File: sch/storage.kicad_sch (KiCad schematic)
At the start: 6 parts, among them J2 Micro_SD_Card, U3 ATF1504AS-xAx44, U4 74LVC125

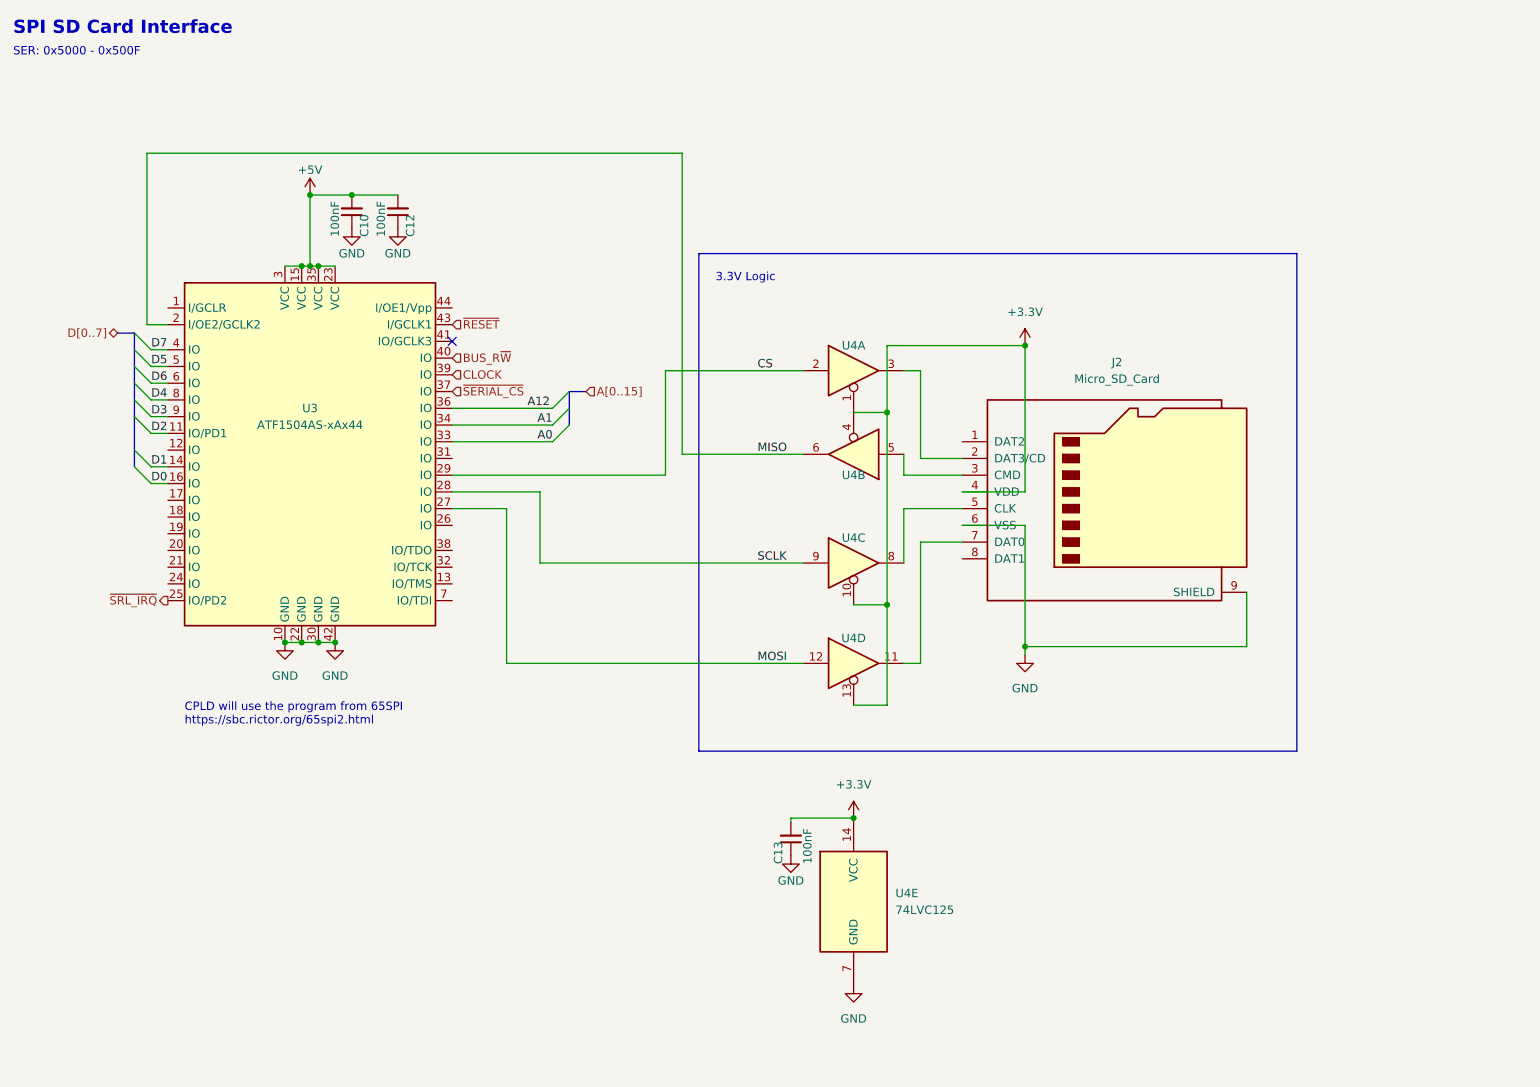
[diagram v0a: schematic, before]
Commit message: fix peripherals, add SPI
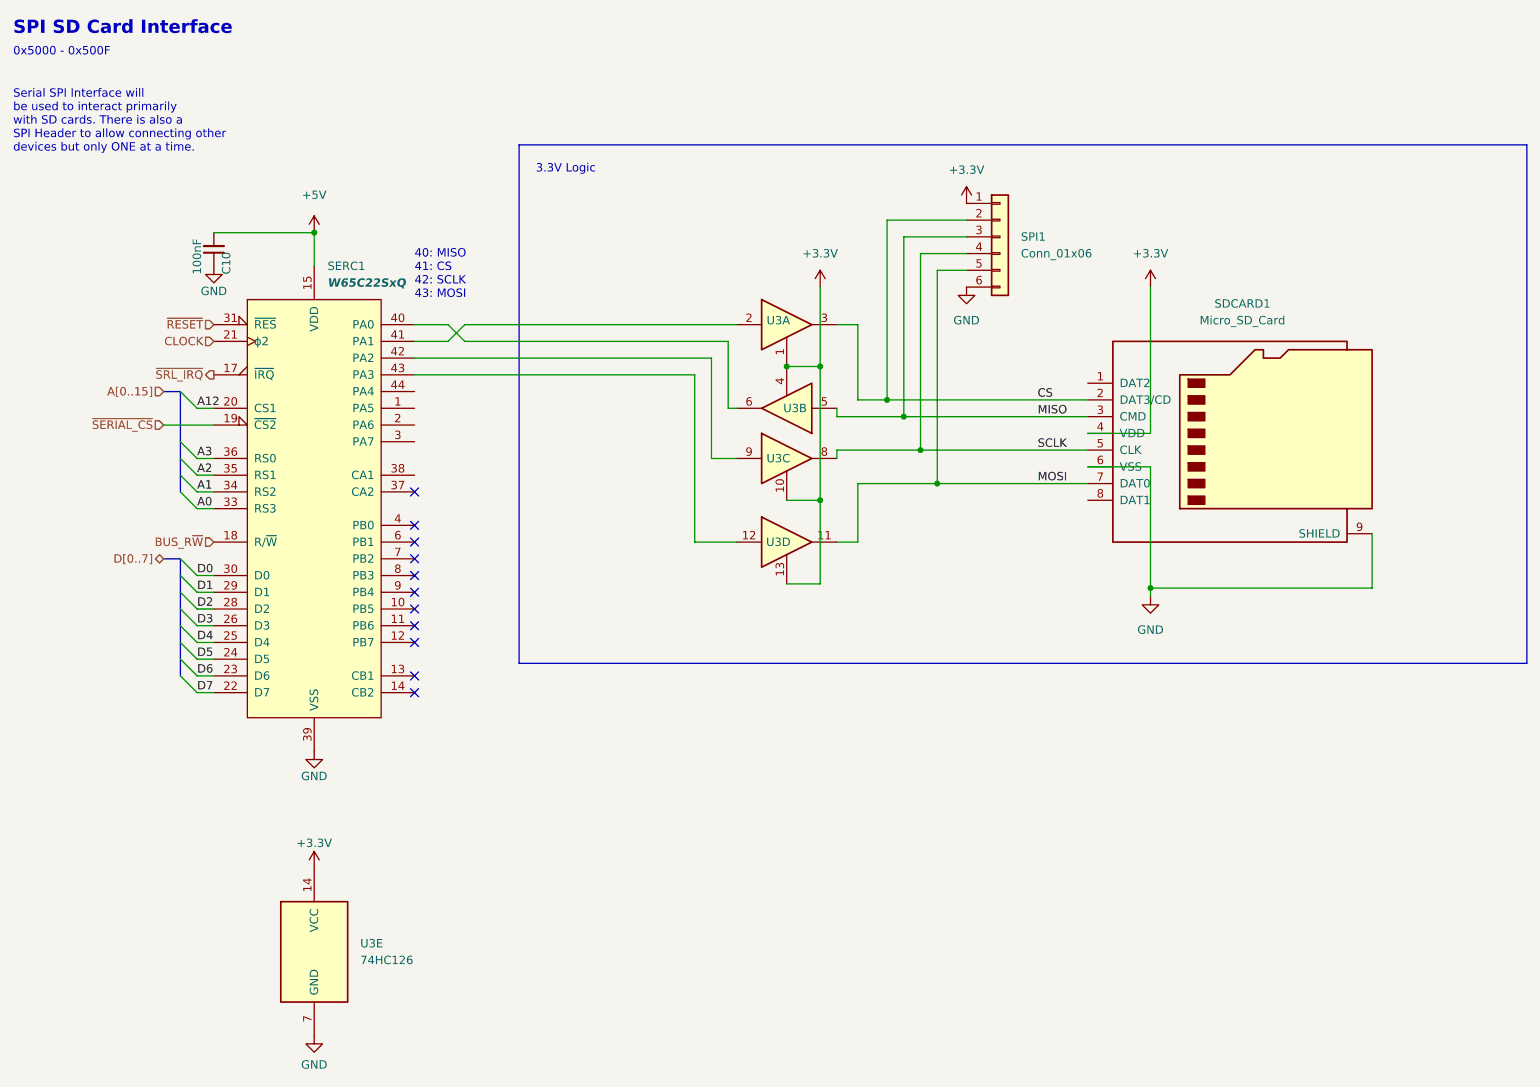
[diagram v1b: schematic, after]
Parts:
- removed C12, C13: 100nF, Capacitor_SMD:C_0805_2012Metric, symbol Device:C_Small
- removed U3: ATF1504AS-xAx44, Package_LCC:PLCC-44, symbol CPLD_Microchip:ATF1504AS-xAx44
- removed U4: 74LVC125, symbol 74xx:74LVC125
- added SERC1: W65C22SxQ, Package_QFP:PQFP-44_10x10mm_P0.8mm, symbol 65xx:W65C22SxQ
- added SPI1: Conn_01x06, Connector_PinHeader_2.00mm:PinHeader_1x06_P2.00mm_Vertical, symbol Connector_Generic:Conn_01x06
- added U3: 74HC126, symbol 74xx:74LS126
- renumbered J2 to SDCARD1
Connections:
- net +3V3: now also SPI1.1 (Pin_1), U3.1, U3.10, U3.13, U3.14 (VCC), U3.4
- net +5V: now also SERC1.15 (VDD)
- net A0: now also SERC1.33 (RS3)
- net A1: now also SERC1.34 (RS2)
- net A12: now also SERC1.20 (CS1)
- net BUS_R~{W}: now also SERC1.18 (R/~{W})
- net CLOCK: now also SERC1.21 (ϕ2)
- net CS: now also SDCARD1.2 (DAT3/CD), SPI1.2 (Pin_2), U3.3
- net D0: now also SERC1.30 (D0)
- net D1: now also SERC1.29 (D1)
- net D2: now also SERC1.28 (D2)
- net D3: now also SERC1.26 (D3)
- net D4: now also SERC1.25 (D4)
- net D5: now also SERC1.24 (D5)
- net D6: now also SERC1.23 (D6)
- net D7: now also SERC1.22 (D7)
- net GND: now also SERC1.39 (VSS), SPI1.6 (Pin_6), U3.7 (GND)
- net MISO: now also SDCARD1.3 (CMD), SPI1.3 (Pin_3), U3.5
- net MOSI: now also SDCARD1.7 (DAT0), SPI1.5 (Pin_5), U3.11
- net SCLK: now also SDCARD1.5 (CLK), SPI1.4 (Pin_4), U3.8
- net ~{RESET}: now also SERC1.31 (~{RES})
- net ~{SERIAL_CS}: now also SERC1.19 (~{CS2})
- net ~{SRL_IRQ}: now also SERC1.17 (~{IRQ})
- new net: SERC1.43 (PA3), U3.12
- new net: SERC1.40 (PA0), U3.6
- new net: SERC1.41 (PA1), U3.2
- new net: SERC1.42 (PA2), U3.9
- new net A2: SERC1.35 (RS1)
- new net A3: SERC1.36 (RS0)
- no-connect marks 1 -> 11
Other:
- note added: "0x5000 - 0x500F"
- note added: "40: MISO 41: CS 42: SCLK 43: MOSI"
- note added: "Serial SPI Interface will be used to interact primarily with SD cards. There is also a SPI Header to allow connecting other devices but only ONE at a time."
- note removed: "CPLD will use the program from 65SPI https://sbc.rictor.org/65spi2.html"
- note removed: "SER: 0x5000 - 0x500F"
- moved on the sheet: C10, SDCARD1

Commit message: Cleanup board
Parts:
- U3: value 74HC126 -> (none)
- U3: value 74HC126 -> (none); footprint Package_SO:SOIC-14_3.9x8.7mm_P1.27mm -> (none)
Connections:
- no-connect marks 11 -> 18
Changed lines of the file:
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@@
   (no_connect (at 86.36 109.855))
   (no_connect (at 86.36 112.395))
+  (no_connect (at 86.36 94.615))
+  (no_connect (at 86.36 81.915))
+  (no_connect (at 86.36 84.455))
+  (no_connect (at 86.36 86.995))
+  (no_connect (at 86.36 89.535))
+  (no_connect (at 188.595 98.425))
+  (no_connect (at 188.595 80.645))
   (bus_entry (at 50.8 122.555) (size 2.54 2.54)
     (stroke (width 0) (type default) (color 0 0 0 0))
@@
     (stroke (width 0) (type default) (color 0 0 0 0))
   )
-  (wire (pts (xy 131.445 76.835) (xy 131.445 92.075))
+  (wire (pts (xy 132.715 76.835) (xy 132.715 92.075))
     (stroke (width 0) (type default) (color 0 0 0 0))
   )
@@
     (stroke (width 0) (type default) (color 0 0 0 0))
   )
-  (wire (pts (xy 131.445 92.075) (xy 135.255 92.075))
+  (wire (pts (xy 132.715 92.075) (xy 135.255 92.075))
     (stroke (width 0) (type default) (color 0 0 0 0))
   )
@@
     (stroke (width 0) (type default) (color 0 0 0 0))
   )
-  (wire (pts (xy 86.36 79.375) (xy 128.905 79.375))
+  (wire (pts (xy 86.36 79.375) (xy 130.175 79.375))
     (stroke (width 0) (type default) (color 0 0 0 0))
   )
@@
     (stroke (width 0) (type default) (color 0 0 0 0))
   )
-  (wire (pts (xy 133.985 84.455) (xy 135.255 84.455))
-    (stroke (width 0) (type default) (color 0 0 0 0))
-  )
   (wire (pts (xy 165.735 95.885) (xy 188.595 95.885))
     (stroke (width 0) (type default) (color 0 0 0 0))
   )
-  (wire (pts (xy 128.905 79.375) (xy 128.905 104.775))
+  (wire (pts (xy 130.175 79.375) (xy 130.175 104.775))
     (stroke (width 0) (type default) (color 0 0 0 0))
   )
@@
     (stroke (width 0) (type default) (color 0 0 0 0))
   )
-  (wire (pts (xy 86.36 76.835) (xy 131.445 76.835))
+  (wire (pts (xy 86.36 76.835) (xy 132.715 76.835))
     (stroke (width 0) (type default) (color 0 0 0 0))
   )
@@
     (stroke (width 0) (type default) (color 0 0 0 0))
   )
-  (wire (pts (xy 133.985 74.295) (xy 133.985 84.455))
+  (wire (pts (xy 135.255 74.295) (xy 135.255 84.455))
     (stroke (width 0) (type default) (color 0 0 0 0))
   )
@@
     (stroke (width 0) (type default) (color 0 0 0 0))
   )
-  (wire (pts (xy 128.905 104.775) (xy 135.255 104.775))
+  (wire (pts (xy 130.175 104.775) (xy 135.255 104.775))
     (stroke (width 0) (type default) (color 0 0 0 0))
   )
@@
     (stroke (width 0) (type default) (color 0 0 0 0))
   )
-  (wire (pts (xy 93.98 74.295) (xy 133.985 74.295))
+  (wire (pts (xy 93.98 74.295) (xy 135.255 74.295))
     (stroke (width 0) (type default) (color 0 0 0 0))
   )
@@
     (in_bom yes) (on_board yes)
     (property "Reference" "U3" (id 0) (at 141.605 104.775 0))
-    (property "Value" "74HC126" (id 1) (at 142.875 98.425 0)
+    (property "Value" "" (id 1) (at 142.875 98.425 0)
       (effects (font (size 1.27 1.27)) hide)
     )
@@
       (effects (font (size 1.27 1.27)) hide)
     )
-    (property "Datasheet" "http://www.ti.com/lit/gpn/sn74LS126" (id 3) (at 142.875 104.775 0)
+    (property "Datasheet" "https://www.ti.com/lit/ds/symlink/sn74lvc126a.pdf" (id 3) (at 142.875 104.775 0)
       (effects (font (size 1.27 1.27)) hide)
     )
@@
     (in_bom yes) (on_board yes)
     (property "Reference" "U3" (id 0) (at 144.145 84.455 0))
-    (property "Value" "74HC126" (id 1) (at 142.875 90.805 0)
+    (property "Value" "" (id 1) (at 142.875 90.805 0)
       (effects (font (size 1.27 1.27)) hide)
     )
@@
       (effects (font (size 1.27 1.27)) hide)
     )
-    (property "Datasheet" "http://www.ti.com/lit/gpn/sn74LS126" (id 3) (at 142.875 84.455 0)
+    (property "Datasheet" "https://www.ti.com/lit/ds/symlink/sn74lvc126a.pdf" (id 3) (at 142.875 84.455 0)
       (effects (font (size 1.27 1.27)) hide)
     )
@@
     (in_bom yes) (on_board yes)
     (property "Reference" "U3" (id 0) (at 141.605 71.12 0))
-    (property "Value" "74HC126" (id 1) (at 142.875 64.77 0)
+    (property "Value" "" (id 1) (at 142.875 64.77 0)
       (effects (font (size 1.27 1.27)) hide)
     )
@@
       (effects (font (size 1.27 1.27)) hide)
     )
-    (property "Datasheet" "http://www.ti.com/lit/gpn/sn74LS126" (id 3) (at 142.875 71.755 0)
+    (property "Datasheet" "https://www.ti.com/lit/ds/symlink/sn74lvc126a.pdf" (id 3) (at 142.875 71.755 0)
       (effects (font (size 1.27 1.27)) hide)
     )
@@
       (effects (font (size 1.27 1.27)) (justify left))
     )
-    (property "Value" "74HC126" (id 1) (at 78.105 168.2749 0)
+    (property "Value" "" (id 1) (at 78.105 168.2749 0)
       (effects (font (size 1.27 1.27)) (justify left))
     )
-    (property "Footprint" "Package_SO:SOIC-14_3.9x8.7mm_P1.27mm" (id 2) (at 71.12 167.005 0)
-      (effects (font (size 1.27 1.27)) hide)
-    )
-    (property "Datasheet" "http://www.ti.com/lit/gpn/sn74LS126" (id 3) (at 71.12 167.005 0)
+    (property "Footprint" "" (id 2) (at 71.12 167.005 0)
+      (effects (font (size 1.27 1.27)) hide)
+    )
+    (property "Datasheet" "https://www.ti.com/lit/ds/symlink/sn74lvc126a.pdf" (id 3) (at 71.12 167.005 0)
       (effects (font (size 1.27 1.27)) hide)
     )
@@
     (in_bom yes) (on_board yes)
     (property "Reference" "U3" (id 0) (at 141.605 92.075 0))
-    (property "Value" "74HC126" (id 1) (at 142.875 85.725 0)
+    (property "Value" "" (id 1) (at 142.875 85.725 0)
       (effects (font (size 1.27 1.27)) hide)
     )
@@
       (effects (font (size 1.27 1.27)) hide)
     )
-    (property "Datasheet" "http://www.ti.com/lit/gpn/sn74LS126" (id 3) (at 142.875 92.075 0)
-      (effects (font (size 1.27 1.27)) hide)
-    )
+    (property "Datasheet" "https://www.ti.com/lit/ds/symlink/sn74lvc126a.pdf" (id 3) (at 142.875 92.075 0)
+      (effects (font (size 1.27 1.27)) hide)
+    )

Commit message: Clearances
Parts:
- U3: value (none) -> 74HC126; footprint (none) -> Package_SO:SOIC-14_3.9x8.7mm_P1.27mm
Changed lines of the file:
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@@
     (in_bom yes) (on_board yes)
     (property "Reference" "U3" (id 0) (at 141.605 104.775 0))
-    (property "Value" "" (id 1) (at 142.875 98.425 0)
-      (effects (font (size 1.27 1.27)) hide)
-    )
-    (property "Footprint" "" (id 2) (at 142.875 104.775 0)
+    (property "Value" "74HC126" (id 1) (at 142.875 98.425 0)
+      (effects (font (size 1.27 1.27)) hide)
+    )
+    (property "Footprint" "Package_SO:SOIC-14_3.9x8.7mm_P1.27mm" (id 2) (at 142.875 104.775 0)
       (effects (font (size 1.27 1.27)) hide)
     )
@@
     (in_bom yes) (on_board yes)
     (property "Reference" "U3" (id 0) (at 144.145 84.455 0))
-    (property "Value" "" (id 1) (at 142.875 90.805 0)
-      (effects (font (size 1.27 1.27)) hide)
-    )
-    (property "Footprint" "" (id 2) (at 142.875 84.455 0)
+    (property "Value" "74HC126" (id 1) (at 142.875 90.805 0)
+      (effects (font (size 1.27 1.27)) hide)
+    )
+    (property "Footprint" "Package_SO:SOIC-14_3.9x8.7mm_P1.27mm" (id 2) (at 142.875 84.455 0)
       (effects (font (size 1.27 1.27)) hide)
     )
@@
     (in_bom yes) (on_board yes)
     (property "Reference" "U3" (id 0) (at 141.605 71.12 0))
-    (property "Value" "" (id 1) (at 142.875 64.77 0)
-      (effects (font (size 1.27 1.27)) hide)
-    )
-    (property "Footprint" "" (id 2) (at 142.875 71.755 0)
+    (property "Value" "74HC126" (id 1) (at 142.875 64.77 0)
+      (effects (font (size 1.27 1.27)) hide)
+    )
+    (property "Footprint" "Package_SO:SOIC-14_3.9x8.7mm_P1.27mm" (id 2) (at 142.875 71.755 0)
       (effects (font (size 1.27 1.27)) hide)
     )
@@
       (effects (font (size 1.27 1.27)) (justify left))
     )
-    (property "Value" "" (id 1) (at 78.105 168.2749 0)
-      (effects (font (size 1.27 1.27)) (justify left))
-    )
-    (property "Footprint" "" (id 2) (at 71.12 167.005 0)
+    (property "Value" "74HC126" (id 1) (at 78.105 168.2749 0)
+      (effects (font (size 1.27 1.27)) (justify left))
+    )
+    (property "Footprint" "Package_SO:SOIC-14_3.9x8.7mm_P1.27mm" (id 2) (at 71.12 167.005 0)
       (effects (font (size 1.27 1.27)) hide)
     )
@@
     (in_bom yes) (on_board yes)
     (property "Reference" "U3" (id 0) (at 141.605 92.075 0))
-    (property "Value" "" (id 1) (at 142.875 85.725 0)
-      (effects (font (size 1.27 1.27)) hide)
-    )
-    (property "Footprint" "" (id 2) (at 142.875 92.075 0)
-      (effects (font (size 1.27 1.27)) hide)
-    )
+    (property "Value" "74HC126" (id 1) (at 142.875 85.725 0)
+      (effects (font (size 1.27 1.27)) hide)
+    )
+    (property "Footprint" "Package_SO:SOIC-14_3.9x8.7mm_P1.27mm" (id 2) (at 142.875 92.075 0)
+      (effects (font (size 1.27 1.27)) hide)
+    )

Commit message: bigger header pins
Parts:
- SPI1: value Conn_01x06 -> (none); footprint Connector_PinHeader_2.00mm:PinHeader_1x06_P2.00mm_Vertical -> (none)
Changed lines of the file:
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@@
       (effects (font (size 1.27 1.27)) (justify left))
     )
-    (property "Value" "Conn_01x06" (id 1) (at 178.435 60.9599 0)
+    (property "Value" "" (id 1) (at 178.435 60.9599 0)
       (effects (font (size 1.27 1.27)) (justify left))
     )
-    (property "Footprint" "Connector_PinHeader_2.00mm:PinHeader_1x06_P2.00mm_Vertical" (id 2) (at 175.26 58.42 0)
+    (property "Footprint" "" (id 2) (at 175.26 58.42 0)
       (effects (font (size 1.27 1.27)) hide)
     )

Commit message: small updates
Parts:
- SPI1: value (none) -> Conn_01x06; footprint (none) -> Connector_PinHeader_2.54mm:PinHeader_1x06_P2.54mm_Vertical
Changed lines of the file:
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@@
       (effects (font (size 1.27 1.27)) (justify left))
     )
-    (property "Value" "" (id 1) (at 178.435 60.9599 0)
+    (property "Value" "Conn_01x06" (id 1) (at 178.435 60.9599 0)
       (effects (font (size 1.27 1.27)) (justify left))
     )
-    (property "Footprint" "" (id 2) (at 175.26 58.42 0)
+    (property "Footprint" "Connector_PinHeader_2.54mm:PinHeader_1x06_P2.54mm_Vertical" (id 2) (at 175.26 58.42 0)
       (effects (font (size 1.27 1.27)) hide)
     )

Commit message: better file structure
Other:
- company: (none) -> zrthxn
- title: (none) -> 8puter
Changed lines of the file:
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@@
 (kicad_sch (version 20211123) (generator eeschema)
   (paper "A4")
+  (title_block
+    (title "8puter")
+    (rev "1.0")
+    (company "zrthxn")
+  )
   (junction (at 158.115 83.185) (diameter 0) (color 0 0 0 0)
   )
